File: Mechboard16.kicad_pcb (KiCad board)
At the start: 2 copper layers, 386.1 x 97 mm, 244 parts, among them CN1 CONN_C16, CN2 CONN_+4, J201 USB_B, J202 CONN_ICSP, J203 CONN_MRESET, J204 CONN_LED, SW0:0 KEY_DEL, SW0:1 KEY_RET, SW0:2 KEY_PND, SW0:3 KEY_HLP, SW0:4 KEY_F1, SW0:5 KEY_F2, SW0:6 KEY_F3, SW0:7 KEY_AT, SW1:0 KEY_3, SW1:1 KEY_W, SW1:2 KEY_A, SW1:3 KEY_4, SW1:4 KEY_Z, SW1:5 KEY_S, SW1:6 KEY_E, SW1:7 KEY_LSH, SW1B:7 KEY_RSH, SW1C:7 KEY_CLK, SW201 SW_RESET, SW2:0 KEY_5, SW2:1 KEY_R, SW2:2 KEY_D, SW2:3 KEY_6, SW2:4 KEY_C, SW2:5 KEY_F, SW2:6 KEY_T, SW2:7 KEY_X, SW3:0 KEY_7, SW3:1 KEY_Y, SW3:2 KEY_G, SW3:3 KEY_8, SW3:4 KEY_B, SW3:5 KEY_H, SW3:6 KEY_U, SW3:7 KEY_V, SW4:0 KEY_9, SW4:1 KEY_I, SW4:2 KEY_J, SW4:3 KEY_0, SW4:4 KEY_M, SW4:5 KEY_K, SW4:6 KEY_O, SW4:7 KEY_N, SW5:0 KEY_DN, SW5:1 KEY_P, SW5:2 KEY_L, SW5:3 KEY_UP, SW5:4 KEY_DOT, SW5:5 KEY_COL, SW5:6 KEY_MIN, SW5:7 KEY_COM, SW6:0 KEY_LF, SW6:1 KEY_AST, SW6:2 KEY_SEM, SW6:3 KEY_RT, SW6:4 KEY_ESC, SW6:5 KEY_EQ, SW6:6 KEY_PLS, SW6:7 KEY_SLA, SW7:0 KEY_1, SW7:1 KEY_CLR, SW7:2 KEY_CTL, SW7:3 KEY_2, SW7:4 KEY_SPC, SW7:5 KEY_CMD, SW7:6 KEY_Q, SW7:7 KEY_RUN, U1 4066, U2 NE555, U201 ATmega32U4-AU, U202 MAX7221, Y201 16M, Y202 16M

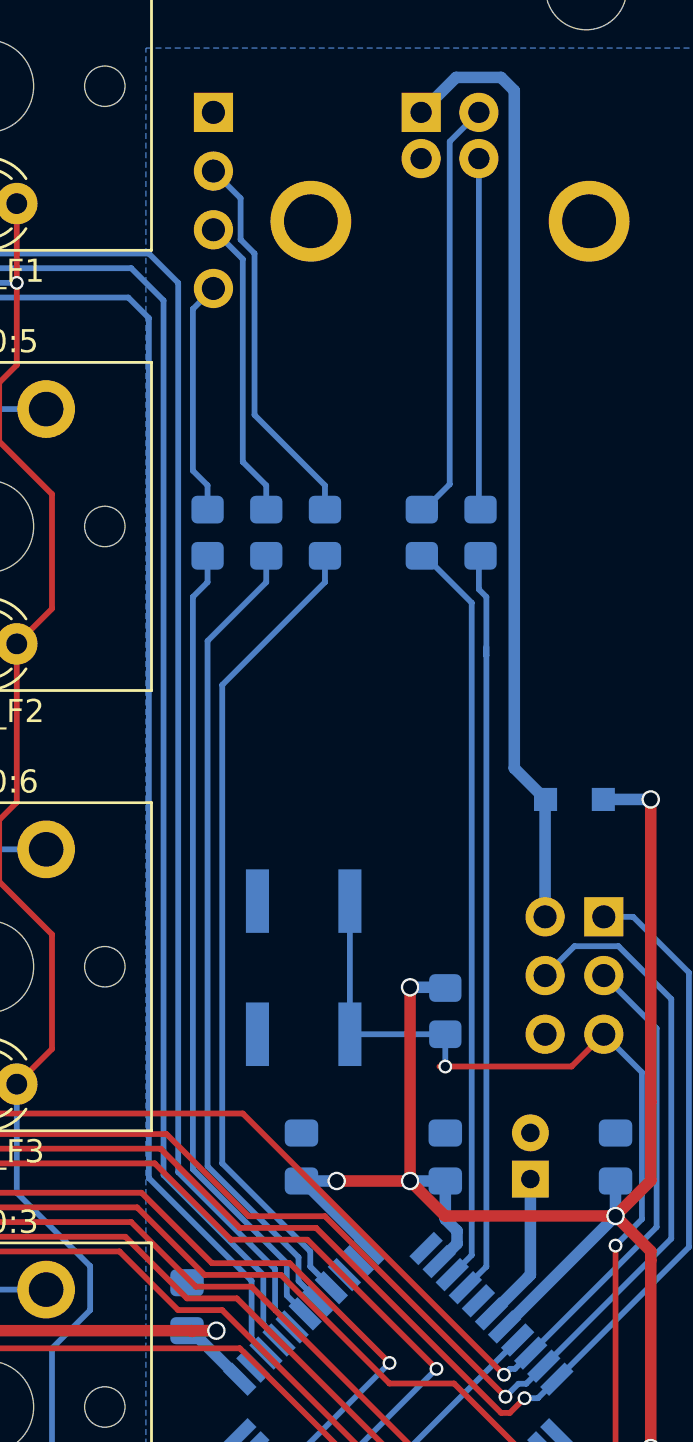
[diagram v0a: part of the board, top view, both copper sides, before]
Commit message: Move SMD resistors
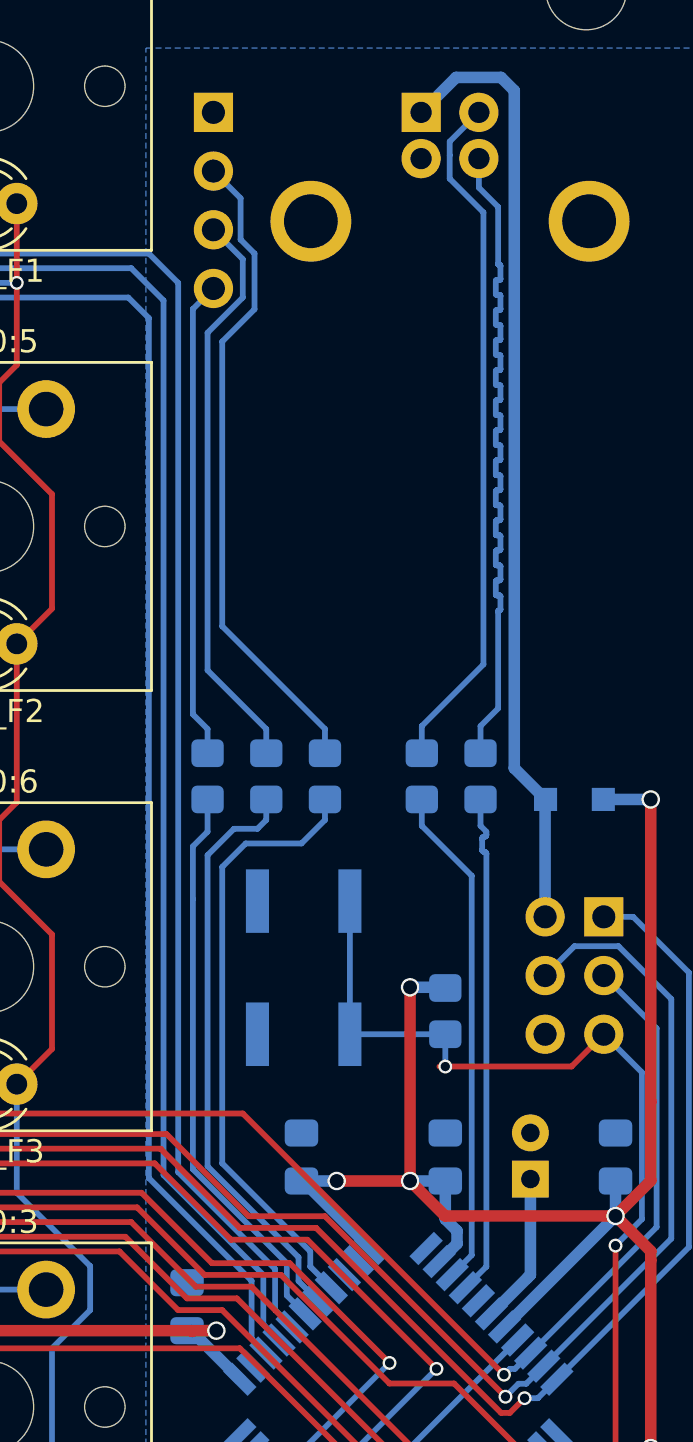
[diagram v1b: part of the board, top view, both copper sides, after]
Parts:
- moved R202 10.5 mm to (395.5, 68.0)
- moved R203 10.5 mm to (392.9, 68.0)
- moved R204 10.5 mm to (388.7, 68.0)
- moved R205 10.5 mm to (386.2, 68.0)
- moved R206 10.5 mm to (383.7, 68.0)
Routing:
- net /USB Controller/u+: track 15.2 -> 30.0 mm
- net Net-(J204-Pad3): track 13.1 -> 24.9 mm
- net Net-(J204-Pad2): track 16.6 -> 28.3 mm
- net /USB Controller/u-: track 18.3 -> 30.0 mm
- net /USB Controller/usb+: track 32.6 -> 21.8 mm
- net /USB Controller/usb-: track 32.5 -> 21.8 mm
- net Net-(J204-Pad4): track 10.2 -> 20.7 mm
- net /USB Controller/st_le_b: track 35.1 -> 24.5 mm
- net /USB Controller/st_led_g: track 35.3 -> 25.3 mm
- net /USB Controller/st_led_r: track 35.5 -> 26.3 mm

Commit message: Happy?
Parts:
- added LD1B:7: LED_RSH, LED_THT:LED_D3.0mm, F.Cu at (279.9, 100.3)
- added LD7A:4: LED_SPC1, LED_THT:LED_D3.0mm, F.Cu at (111.0, 119.4)
- added LD7C:4: LED_SPC3, LED_THT:LED_D3.0mm, F.Cu at (211.1, 119.4)
- added Q201: MMBT3904, Package_TO_SOT_SMD:SOT-23, B.Cu at (68.4, 100.4)
- added Q202: MMBT3904, Package_TO_SOT_SMD:SOT-23, B.Cu at (168.6, 119.0)
- added R5: 1k, Resistor_SMD:R_0805_2012Metric_Pad1.20x1.40mm_HandSolder, B.Cu at (57.3, 100.3)
- added R6: 1k, Resistor_SMD:R_0805_2012Metric_Pad1.20x1.40mm_HandSolder, B.Cu at (276.4, 100.3)
- added R7: 1k, Resistor_SMD:R_0805_2012Metric_Pad1.20x1.40mm_HandSolder, B.Cu at (107.5, 119.4)
- added R8: 1k, Resistor_SMD:R_0805_2012Metric_Pad1.20x1.40mm_HandSolder, B.Cu at (157.4, 119.4)
- added R9: 1k, Resistor_SMD:R_0805_2012Metric_Pad1.20x1.40mm_HandSolder, B.Cu at (207.5, 119.4)
- LD7B:4: renamed from LD7:4; value LED_SPC -> LED_SPC2
- moved LD7B:4 0.06 mm to (161.0, 119.4)
- moved SW7:4 0.06 mm to (162.2, 114.3)
- renumbered LD1:7 to LD1A:7
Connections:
- LD1A:7 pad 1: /USB Controller/lcol7 -> Net-(LD1A:7-Pad1)
- LD1A:7 pad 2: /USB Controller/lrow1 -> Net-(LD1A:7-Pad2)
- LD7B:4 pad 1: /USB Controller/lcol4 -> Net-(LD7B:4-Pad1)
- LD7B:4 pad 2: /USB Controller/lrow7 -> Net-(LD7A:4-Pad2)
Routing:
- net Net-(LD1A:7-Pad2): track 0.00 -> 229.6 mm, vias 0 -> 2
- net Net-(LD7A:4-Pad2): track 0.00 -> 109.6 mm, vias 0 -> 2
- net /USB Controller/lcol4: track 486.1 -> 590.6 mm, vias 5 -> 6
- net /USB Controller/lcol7: track 418.7 -> 443.8 mm, vias 2 -> 3
- net +5V: track 630.1 -> 649.9 mm, vias 13 -> 15
- net /USB Controller/lrow1: track 403.9 -> 397.4 mm
- net Net-(LD1A:7-Pad1): track 0.00 -> 2.54 mm
- net Net-(LD7B:4-Pad1): track 0.00 -> 2.54 mm
- net Net-(LD7C:4-Pad1): track 0.00 -> 2.54 mm
- net Net-(LD1B:7-Pad1): track 0.00 -> 2.54 mm
- net Net-(LD7A:4-Pad1): track 0.00 -> 2.54 mm
- net col7: track 458.4 -> 459.9 mm
- net /USB Controller/lrow7: track 478.7 -> 477.3 mm, vias 3 -> 4
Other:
- board text added: "USB & LED CONTROLLER"

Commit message: Finaaaaaaaaaal touches
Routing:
- net GND: track 476.0 -> 477.4 mm
- net +5V: track 649.9 -> 651.1 mm
- net /USB Controller/lcol4: track 590.6 -> 591.4 mm

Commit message: IN PRODUCTION!
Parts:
- D201: value 1n4148 -> 1n5819; footprint Diode_SMD:D_SOD-323_HandSoldering -> Diode_SMD:D_SMA
- R207: value 22k -> 220k
- R3: value 56 -> 1k
- moved D201 0.73 mm to (400.3, 69.0)
- renumbered R7 to R208, R8 to R209, R9 to R210, R5 to R211, R6 to R212
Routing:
- net +5V: track 651.1 -> 647.1 mm

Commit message: R4 ready for hybrid MX/Matias switches and fix some inconsitencies in routing
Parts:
- renumbered C211 to C207, C207 to C208, C208 to C209, C209 to C210, C210 to C211
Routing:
- net col3: track 429.4 -> 445.7 mm
- net row0: track 376.3 -> 379.5 mm
- net /USB Controller/lcol5: track 447.2 -> 445.2 mm
- net /USB Controller/lrow6: track 504.6 -> 506.0 mm
- net row1: track 563.6 -> 564.9 mm
- net col5: track 723.0 -> 721.8 mm
- net col1: track 424.8 -> 423.7 mm
- net row4: track 394.8 -> 393.8 mm
- net col6: track 445.1 -> 444.3 mm
- net /USB Controller/lcol2: track 395.2 -> 394.5 mm
- net /USB Controller/lrow2: track 358.7 -> 358.1 mm
- net /USB Controller/lcol7: track 443.8 -> 444.3 mm

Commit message: R3 done
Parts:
- SW0:0, SW0:2, SW0:7, SW1:0, SW1:1, SW1:2, SW1:3, SW1:4, SW1:5, SW1:6, SW1C:7, SW2:0, SW2:1, SW2:2, SW2:3, SW2:4, SW2:5, SW2:6, SW2:7, SW3:0, SW3:1, SW3:2, SW3:3, SW3:4, SW3:5, SW3:6, SW3:7, SW4:0, SW4:1, SW4:2, SW4:3, SW4:4, SW4:5, SW4:6, SW4:7, SW5:0, SW5:1, SW5:2, SW5:3, SW5:4, SW5:5, SW5:6, SW5:7, SW6:0, SW6:1, SW6:2, SW6:3, SW6:4, SW6:5, SW6:6, SW6:7, SW7:0, SW7:1, SW7:3, SW7:5, SW7:6, SW7:7: footprint Mechboard16:SW_Cherry_MX_PCB_1.00u -> Mechboard16:SW_Hybrid_Cherry_MX_Alps_1.00u
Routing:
- net col6: track 444.3 -> 460.4 mm
- net /USB Controller/lrow6: track 506.0 -> 490.3 mm, vias 2 -> 3
- net row0: track 379.5 -> 383.9 mm
- net /USB Controller/lrow5: track 245.9 -> 244.7 mm
- net col5: track 721.8 -> 722.6 mm
- net row1: track 564.9 -> 564.4 mm
- net /USB Controller/lrow2: track 358.1 -> 357.5 mm
- net /USB Controller/lrow4: track 278.3 -> 277.8 mm
- net /USB Controller/lrow1: track 397.6 -> 397.1 mm
- net /USB Controller/lcol0: track 306.1 -> 305.6 mm

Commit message: R2 done
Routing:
- net col5: track 722.6 -> 733.0 mm
- net col2: track 481.3 -> 482.3 mm
